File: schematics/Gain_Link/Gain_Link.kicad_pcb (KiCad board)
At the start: 4 copper layers, 79.2 x 84.2 mm, 29 parts, among them J1 PCIE-036-02-X-D-TH, J2 Conn_02x02_Odd_Even, J3 Conn_02x02_Odd_Even, U1 INA849D, U2 INA849D

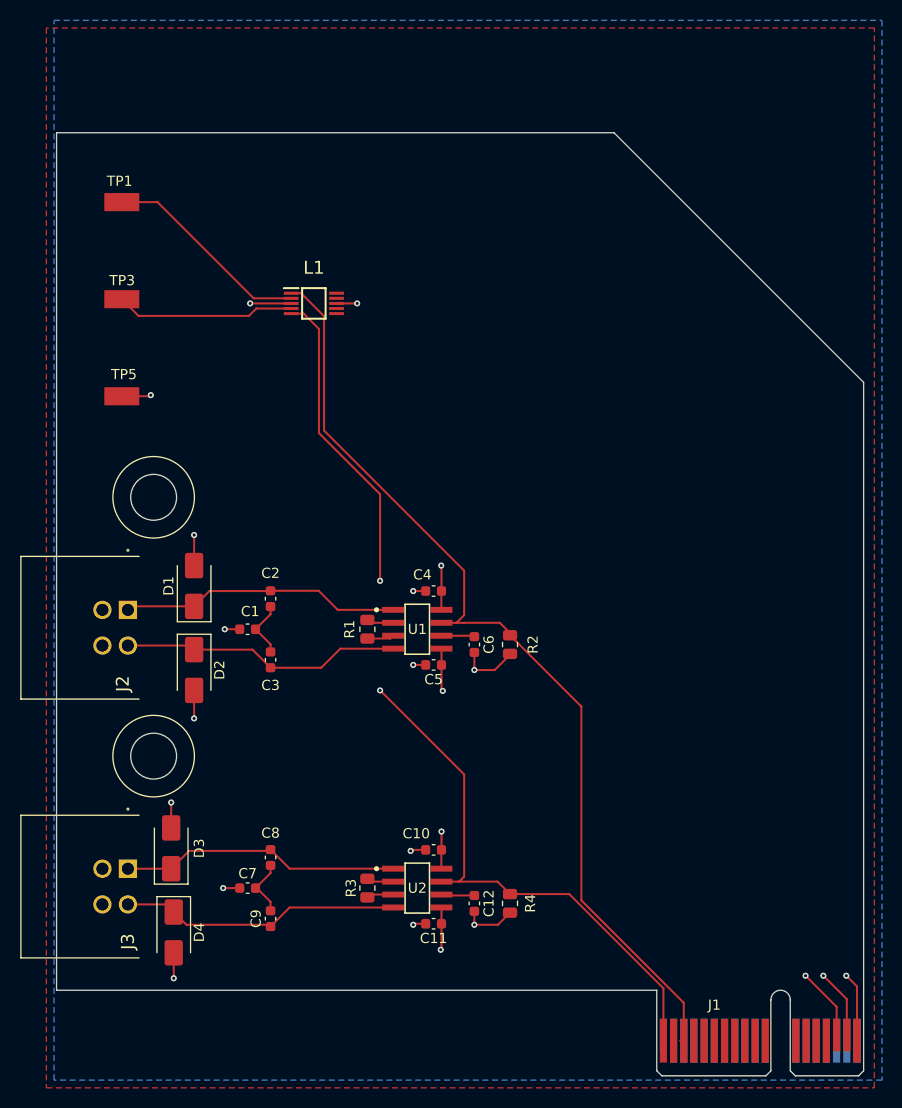
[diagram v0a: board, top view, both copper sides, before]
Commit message: fix board dims, update tp numbers
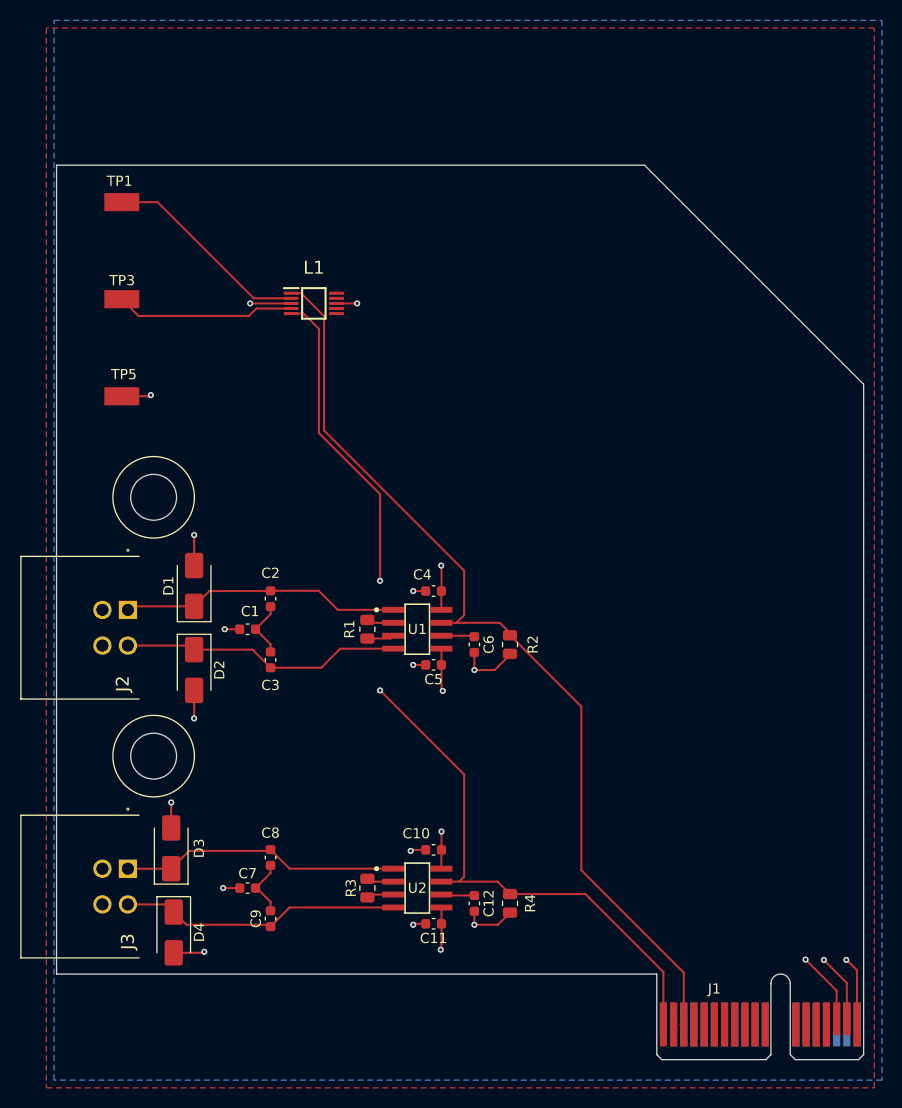
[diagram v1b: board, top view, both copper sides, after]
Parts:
- moved J1 1.59 mm to (151.4, 127.6)
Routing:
- net /S_{1out}: track 94.8 -> 93.2 mm
- net /S_{2out}: track 95.0 -> 94.3 mm
- net GND: track 41.8 -> 42.4 mm
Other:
- board size 79.2 x 84.2 mm -> 79.2 x 79.4 mm
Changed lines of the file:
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@@
 	(footprint "Connector_PCBEdge:BUS_PCIexpress_x1"
 		(layer "F.Cu")
-		(at 151.4 129.175)
+		(at 151.4 127.5875)
 		(descr "PCIexpress Bus Edge Connector x1 http://www.ritrontek.com/uploadfile/2016/1026/20161026105231124.pdf#page=70")
 		(tags "PCIe")
@@
 	)
 	(gr_line
-		(start 92.5 129.175)
-		(end 92.5 45.025)
+		(start 92.5 127.5875)
+		(end 92.5 48.2125)
 		(stroke
 			(width 0.05)
-			(type default)
+			(type solid)
 		)
 		(layer "Edge.Cuts")
 	)
 	(gr_line
-		(start 147.2 45.025)
-		(end 171.7 69.525)
-		(stroke
-			(width 0.05)
-			(type default)
-		)
-		(layer "Edge.Cuts")
-	)
-	(gr_line
-		(start 92.5 45.025)
-		(end 147.2 45.025)
+		(start 92.5 48.2125)
+		(end 150.2 48.2125)
 		(stroke
 			(width 0.05)
@@
 	)
 	(gr_line
-		(start 151.4 129.175)
-		(end 92.5 129.175)
+		(start 150.2 48.2125)
+		(end 171.7 69.711005)
+		(stroke
+			(width 0.05)
+			(type default)
+		)
+		(layer "Edge.Cuts")
+	)
+	(gr_line
+		(start 151.4 127.5875)
+		(end 92.5 127.5875)
 		(stroke
 			(width 0.05)
@@
 	)
 	(gr_line
-		(start 171.7 129.175)
-		(end 171.7 69.525)
+		(start 171.7 127.5875)
+		(end 171.7 69.711005)
 		(stroke
 			(width 0.05)
@@
 	)
 	(segment
-		(start 171.05 128.8)
-		(end 170 127.75)
+		(start 171.05 127.2125)
+		(end 170 126.1625)
 		(width 0.2)
 		(layer "F.Cu")
@@
 	)
 	(segment
+		(start 106.9 125.5)
+		(end 107 125.4)
+		(width 0.2)
+		(layer "F.Cu")
+		(net 1)
+	)
+	(segment
 		(start 133.5 96.275)
 		(end 133.5 97.75)
@@
 	)
 	(segment
+		(start 170 126.1625)
+		(end 170 126.2)
+		(width 0.2)
+		(layer "F.Cu")
+		(net 1)
+	)
+	(segment
 		(start 127.35 115.4)
 		(end 127.25 115.5)
@@
 	)
 	(segment
-		(start 104 125.5)
-		(end 104 128)
-		(width 0.2)
-		(layer "F.Cu")
-		(net 1)
-	)
-	(segment
 		(start 103.75 113.25)
 		(end 103.75 110.75)
@@
 	)
 	(segment
-		(start 171.05 134.125)
-		(end 171.05 128.8)
+		(start 171.05 132.5375)
+		(end 171.05 127.2125)
 		(width 0.2)
 		(layer "F.Cu")
@@
 		(start 137 96.25)
 		(end 135.5 97.75)
+		(width 0.2)
+		(layer "F.Cu")
+		(net 1)
+	)
+	(segment
+		(start 104 125.5)
+		(end 106.9 125.5)
 		(width 0.2)
 		(layer "F.Cu")
@@
 	)
 	(via
+		(at 170 126.2)
+		(size 0.6)
+		(drill 0.3)
+		(layers "F.Cu" "B.Cu")
+		(net 1)
+	)
+	(via
 		(at 106 102.5)
 		(size 0.6)
@@
 	)
 	(via
-		(at 170 127.75)
-		(size 0.6)
-		(drill 0.3)
-		(layers "F.Cu" "B.Cu")
-		(net 1)
-	)
-	(via
 		(at 127.5 97.25)
 		(size 0.6)
@@
 	)
 	(via
-		(at 104 128)
+		(at 107 125.4)
 		(size 0.6)
 		(drill 0.3)
@@
 	)
 	(segment
-		(start 170.05 130.05)
-		(end 170.05 133.575)
+		(start 170.05 128.4625)
+		(end 170.05 131.9875)
 		(width 0.2)
 		(layer "F.Cu")
@@
 	)
 	(segment
-		(start 167.75 127.75)
-		(end 170.05 130.05)
+		(start 167.75 126.1625)
+		(end 170.05 128.4625)
 		(width 0.2)
 		(layer "F.Cu")
@@
 	)
 	(segment
+		(start 167.75 126.1625)
+		(end 167.7625 126.1625)
+		(width 0.2)
+		(layer "F.Cu")
+		(net 3)
+	)
+	(segment
 		(start 130.275 87.525)
 		(end 130.25 87.5)
@@
 	)
 	(segment
+		(start 167.7625 126.1625)
+		(end 167.8 126.2)
+		(width 0.2)
+		(layer "F.Cu")
+		(net 3)
+	)
+	(segment
 		(start 130.275 90)
 		(end 130.275 87.525)
@@
 		(width 0.2)
 		(layer "F.Cu")
-		(net 3)
-	)
-	(via
-		(at 167.75 127.75)
-		(size 0.6)
-		(drill 0.3)
-		(layers "F.Cu" "B.Cu")
 		(net 3)
 	)
@@
 		(net 3)
 	)
+	(via
+		(at 167.8 126.2)
+		(size 0.6)
+		(drill 0.3)
+		(layers "F.Cu" "B.Cu")
+		(net 3)
+	)
 	(segment
 		(start 103.75 117.25)
@@
 	)
 	(segment
+		(start 154.05 127.45)
+		(end 144 117.4)
+		(width 0.2)
+		(layer "F.Cu")
+		(net 10)
+	)
+	(segment
 		(start 131.75 93.115)
 		(end 132.5 92.365)
@@
 	)
 	(segment
-		(start 154.05 130.407958)
-		(end 154.05 134.125)
-		(width 0.2)
-		(layer "F.Cu")
-		(net 10)
-	)
-	(segment
 		(start 132.5 88)
 		(end 132.5 92)
@@
 	)
 	(segment
+		(start 144 117.4)
+		(end 144 101.3375)
+		(width 0.2)
+		(layer "F.Cu")
+		(net 10)
+	)
+	(segment
 		(start 137 94.3375)
 		(end 137 94.115)
@@
 	)
 	(segment
-		(start 137 94.3375)
-		(end 144 101.3375)
+		(start 144 101.3375)
+		(end 137 94.3375)
 		(width 0.2)
 		(layer "F.Cu")
@@
 	)
 	(segment
-		(start 144 120.357958)
-		(end 154.05 130.407958)
-		(width 0.2)
-		(layer "F.Cu")
-		(net 10)
-	)
-	(segment
 		(start 131.75 93.115)
 		(end 130.2636 93.115)
@@
 	)
 	(segment
+		(start 154.05 132.5375)
+		(end 154.05 127.45)
+		(width 0.2)
+		(layer "F.Cu")
+		(net 10)
+	)
+	(segment
 		(start 132.5 93.115)
 		(end 131.75 93.115)
@@
 	)
 	(segment
-		(start 144 101.3375)
-		(end 144 120.357958)
-		(width 0.2)
-		(layer "F.Cu")
-		(net 10)
-	)
-	(segment
-		(start 153.701 134.125)
-		(end 154.05 134.125)
+		(start 153.701 132.5375)
+		(end 154.05 132.5375)
 		(width 0.2)
 		(layer "F.Cu")
@@
 	)
 	(segment
-		(start 142.812442 119.7375)
-		(end 152.05 128.975058)
-		(width 0.2)
-		(layer "F.Cu")
-		(net 13)
-	)
-	(segment
 		(start 132.5 118.015)
 		(end 132 118.515)
@@
 	)
 	(segment
+		(start 144.399942 119.7375)
+		(end 144.731221 120.068779)
+		(width 0.2)
+		(layer "F.Cu")
+		(net 13)
+	)
+	(segment
 		(start 124.25 99.75)
 		(end 132.5 108)
@@
 	)
 	(segment
+		(start 144.731221 120.068779)
+		(end 152.05 127.387558)
+		(width 0.2)
+		(layer "F.Cu")
+		(net 13)
+	)
+	(segment
 		(start 135.7775 118.515)
 		(end 137 119.7375)
@@
 	)
 	(segment
-		(start 137 119.7375)
-		(end 142.812442 119.7375)
-		(width 0.2)
-		(layer "F.Cu")
-		(net 13)
-	)
-	(segment
 		(start 115.5 62.8)
 		(end 115.525 62.775)
@@
 	)
 	(segment
-		(start 152.05 128.975058)
-		(end 152.05 134.125)
+		(start 137 119.7375)
+		(end 144.399942 119.7375)
+		(width 0.2)
+		(layer "F.Cu")
+		(net 13)
+	)
+	(segment
+		(start 152.05 127.387558)
+		(end 152.05 132.5375)
 		(width 0.2)
 		(layer "F.Cu")
@@
 	)
 	(segment
-		(start 166 127.75)
-		(end 169.05 130.8)
+		(start 166 126.1625)
+		(end 169.05 129.2125)
 		(width 0.2)
 		(layer "F.Cu")
@@
 	)
 	(segment
-		(start 169.05 130.8)
-		(end 169.05 134.125)
+		(start 169.05 129.2125)
+		(end 169.05 132.5375)
 		(width 0.2)
 		(layer "F.Cu")
@@
 	)
 	(via
-		(at 166 127.75)
+		(at 166 126.1625)
 		(size 0.6)
 		(drill 0.3)

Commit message: clean repository, add .gitignore
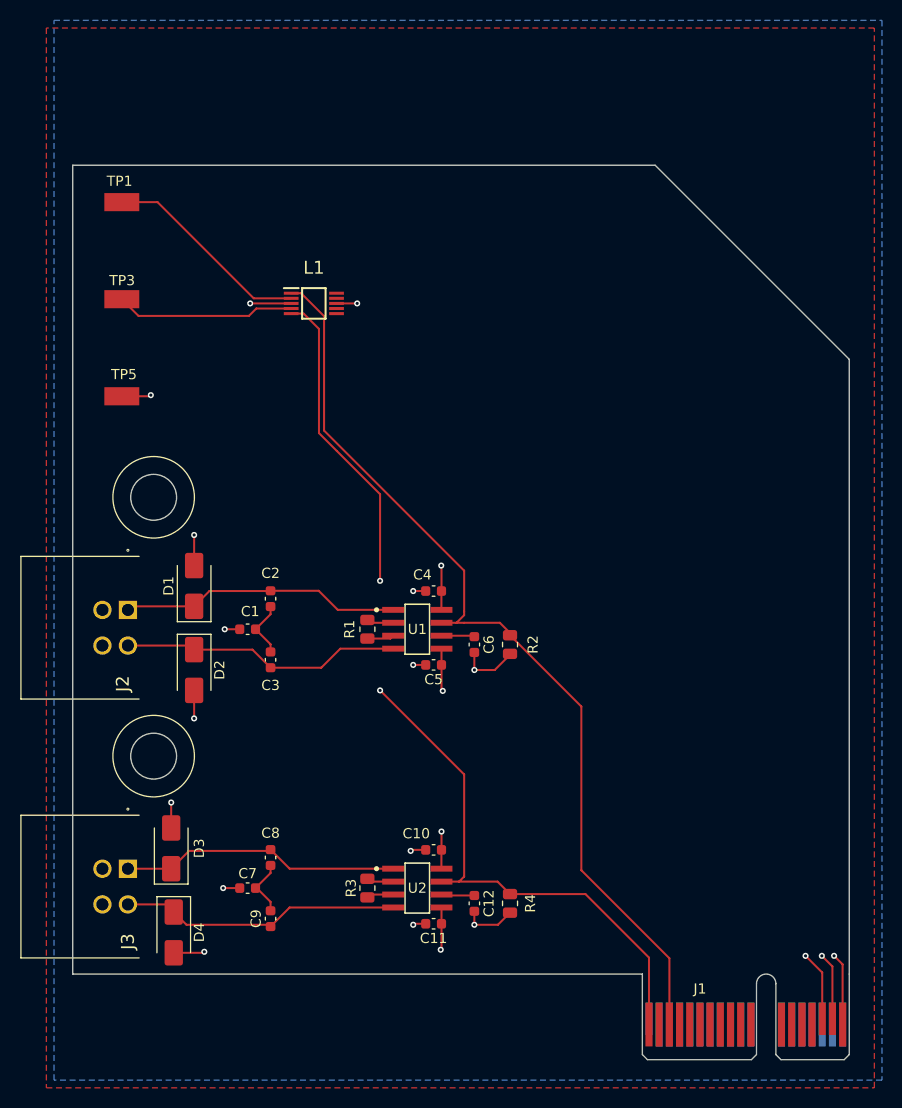
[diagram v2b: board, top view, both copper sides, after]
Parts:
- moved J1 1.41 mm to (150.0, 127.6)
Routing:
- net /S_{1out}: track 93.2 -> 92.3 mm
- net -12V: track 16.0 -> 15.2 mm
- net /S_{2out}: track 94.3 -> 93.8 mm
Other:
- board size 79.2 x 79.4 mm -> 76.2 x 79.4 mm
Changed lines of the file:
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@@
 	(footprint "Connector_PCBEdge:BUS_PCIexpress_x1"
 		(layer "F.Cu")
-		(at 151.4 127.5875)
+		(at 149.9875 127.5875)
 		(descr "PCIexpress Bus Edge Connector x1 http://www.ritrontek.com/uploadfile/2016/1026/20161026105231124.pdf#page=70")
 		(tags "PCIe")
@@
 	)
 	(gr_line
-		(start 92.5 127.5875)
-		(end 92.5 48.2125)
+		(start 94.0875 127.5875)
+		(end 94.0875 48.2125)
 		(stroke
 			(width 0.05)
@@
 	)
 	(gr_line
-		(start 92.5 48.2125)
-		(end 150.2 48.2125)
+		(start 94.0875 48.2125)
+		(end 151.2375 48.2125)
+		(stroke
+			(width 0.05)
+			(type default)
+		)
+		(layer "Edge.Cuts")
+	)
+	(gr_line
+		(start 170.2875 67.2625)
+		(end 151.2375 48.2125)
 		(stroke
 			(width 0.05)
@@
 	)
 	(gr_line
-		(start 150.2 48.2125)
-		(end 171.7 69.711005)
+		(start 170.2875 127.5875)
+		(end 170.2875 67.2625)
 		(stroke
 			(width 0.05)
-			(type default)
+			(type solid)
 		)
 		(layer "Edge.Cuts")
 	)
 	(gr_line
-		(start 151.4 127.5875)
-		(end 92.5 127.5875)
+		(start 94.0875 127.5875)
+		(end 149.9875 127.5875)
 		(stroke
 			(width 0.05)
@@
 		(layer "Edge.Cuts")
 	)
-	(gr_line
-		(start 171.7 127.5875)
-		(end 171.7 69.711005)
-		(stroke
-			(width 0.05)
-			(type default)
-		)
-		(layer "Edge.Cuts")
-	)
-	(segment
-		(start 171.05 127.2125)
-		(end 170 126.1625)
+	(segment
+		(start 169.6375 132.5375)
+		(end 169.6375 126.6375)
 		(width 0.2)
 		(layer "F.Cu")
@@
 	)
 	(segment
-		(start 170 126.1625)
-		(end 170 126.2)
-		(width 0.2)
-		(layer "F.Cu")
-		(net 1)
-	)
-	(segment
 		(start 127.35 115.4)
 		(end 127.25 115.5)
@@
 	)
 	(segment
+		(start 169.6375 126.6375)
+		(end 168.8 125.8)
+		(width 0.2)
+		(layer "F.Cu")
+		(net 1)
+	)
+	(segment
 		(start 128.725 115.4)
 		(end 127.35 115.4)
-		(width 0.2)
-		(layer "F.Cu")
-		(net 1)
-	)
-	(segment
-		(start 171.05 132.5375)
-		(end 171.05 127.2125)
 		(width 0.2)
 		(layer "F.Cu")
@@
 	)
 	(via
-		(at 170 126.2)
-		(size 0.6)
-		(drill 0.3)
-		(layers "F.Cu" "B.Cu")
-		(net 1)
-	)
-	(via
 		(at 106 102.5)
 		(size 0.6)
@@
 	)
 	(via
+		(at 168.8 125.8)
+		(size 0.6)
+		(drill 0.3)
+		(layers "F.Cu" "B.Cu")
+		(net 1)
+	)
+	(via
 		(at 108.85 119.15)
 		(size 0.6)
@@
 	)
 	(segment
-		(start 170.05 128.4625)
-		(end 170.05 131.9875)
+		(start 168.6375 126.8375)
+		(end 168.6375 131.9875)
 		(width 0.2)
 		(layer "F.Cu")
@@
 	)
 	(segment
-		(start 167.75 126.1625)
-		(end 170.05 128.4625)
+		(start 167.6 125.8)
+		(end 168.6375 126.8375)
 		(width 0.2)
 		(layer "F.Cu")
@@
 	)
 	(segment
-		(start 167.75 126.1625)
-		(end 167.7625 126.1625)
-		(width 0.2)
-		(layer "F.Cu")
-		(net 3)
-	)
-	(segment
 		(start 130.275 87.525)
 		(end 130.25 87.5)
@@
 		(start 115.525 61.775)
 		(end 111.5 61.775)
-		(width 0.2)
-		(layer "F.Cu")
-		(net 3)
-	)
-	(segment
-		(start 167.7625 126.1625)
-		(end 167.8 126.2)
 		(width 0.2)
 		(layer "F.Cu")
@@
 	)
 	(via
-		(at 167.8 126.2)
+		(at 167.6 125.8)
 		(size 0.6)
 		(drill 0.3)
@@
 	)
 	(segment
-		(start 154.05 127.45)
-		(end 144 117.4)
-		(width 0.2)
-		(layer "F.Cu")
-		(net 10)
-	)
-	(segment
 		(start 131.75 93.115)
 		(end 132.5 92.365)
@@
 	)
 	(segment
+		(start 144 117.4)
+		(end 152.6375 126.0375)
+		(width 0.2)
+		(layer "F.Cu")
+		(net 10)
+	)
+	(segment
 		(start 132.5 92.365)
 		(end 132.5 92)
@@
 	)
 	(segment
-		(start 154.05 132.5375)
-		(end 154.05 127.45)
+		(start 152.6375 126.0375)
+		(end 152.6375 132.5375)
 		(width 0.2)
 		(layer "F.Cu")
@@
 	)
 	(segment
-		(start 153.701 132.5375)
-		(end 154.05 132.5375)
-		(width 0.2)
-		(layer "F.Cu")
-		(net 10)
-	)
-	(segment
 		(start 120 76.25)
 		(end 124.25 80.5)
@@
 	)
 	(segment
+		(start 150.6375 132.5375)
+		(end 150.6375 125.975058)
+		(width 0.2)
+		(layer "F.Cu")
+		(net 13)
+	)
+	(segment
 		(start 132.5 108)
 		(end 132.5 118.015)
@@
 	)
 	(segment
+		(start 144.399942 119.7375)
+		(end 137 119.7375)
+		(width 0.2)
+		(layer "F.Cu")
+		(net 13)
+	)
+	(segment
 		(start 132.5 118.015)
 		(end 132 118.515)
@@
 	)
 	(segment
-		(start 144.399942 119.7375)
-		(end 144.731221 120.068779)
-		(width 0.2)
-		(layer "F.Cu")
-		(net 13)
-	)
-	(segment
 		(start 124.25 99.75)
 		(end 132.5 108)
@@
 	)
 	(segment
-		(start 144.731221 120.068779)
-		(end 152.05 127.387558)
-		(width 0.2)
-		(layer "F.Cu")
-		(net 13)
-	)
-	(segment
 		(start 135.7775 118.515)
 		(end 137 119.7375)
@@
 	)
 	(segment
+		(start 150.6375 125.975058)
+		(end 144.399942 119.7375)
+		(width 0.2)
+		(layer "F.Cu")
+		(net 13)
+	)
+	(segment
 		(start 120 76.25)
 		(end 118.25 74.5)
-		(width 0.2)
-		(layer "F.Cu")
-		(net 13)
-	)
-	(segment
-		(start 137 119.7375)
-		(end 144.399942 119.7375)
-		(width 0.2)
-		(layer "F.Cu")
-		(net 13)
-	)
-	(segment
-		(start 152.05 127.387558)
-		(end 152.05 132.5375)
 		(width 0.2)
 		(layer "F.Cu")
@@
 	)
 	(segment
+		(start 167.6375 131.9875)
+		(end 167.6375 127.4375)
+		(width 0.2)
+		(layer "F.Cu")
+		(net 51)
+	)
+	(segment
 		(start 130.275 99.675)
 		(end 130.4 99.8)
@@
 	)
 	(segment
-		(start 166 126.1625)
-		(end 169.05 129.2125)
-		(width 0.2)
-		(layer "F.Cu")
-		(net 51)
-	)
-	(segment
 		(start 130.275 95.6664)
 		(end 130.2636 95.655)
@@
 	)
 	(segment
-		(start 169.05 129.2125)
-		(end 169.05 132.5375)
+		(start 167.6375 127.4375)
+		(end 166 125.8)
 		(width 0.2)
 		(layer "F.Cu")
@@
 		(width 0.2)
 		(layer "F.Cu")
-		(net 51)
-	)
-	(via
-		(at 166 126.1625)
-		(size 0.6)
-		(drill 0.3)
-		(layers "F.Cu" "B.Cu")
 		(net 51)
 	)
@@
 		(size 0.6)
 		(drill 0.3)
+		(layers "F.Cu" "B.Cu")
+		(net 51)
+	)
+	(via
+		(at 166 125.8)
+		(size 0.6)
+		(drill 0.3)
